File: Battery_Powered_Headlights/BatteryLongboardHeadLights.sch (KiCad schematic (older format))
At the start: 12 parts, among them U1 AL8805

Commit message: schematic changes nearly done
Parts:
- added C? (x6): C, symbol C
- added D?: D_Schottky, symbol D_Schottky
- added L?: L, symbol L
- added R? (x7): R, symbol R
- added U?: bq29700, MODULE, symbol bq29700
- added U?: MCP73833T, MODULE, symbol MCP73833T
- added U?: TPS55330RTER, MODULE, symbol TPS55330RTER
- added U?: DMN2040LTS-13, MODULE, symbol DMN2040LTS-13
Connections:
- net labels added: +BATT, SWITCH
- net labels removed: CTRL
- wire segments 44 -> 85
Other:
- note added: "Battery Charging and Regulation"
- note added: "Battery Protection"
- note added: "Fix this"
- note added: "LED Headlights"
- note removed: "Jumper to set control of LED's to either\nvoltage divider or external control (MCU)"
- note removed: "White LED Headlights"
- moved on the sheet: C1, C2, C3, C4, D1, D2, D4, L1, R1, R2, R3, U1

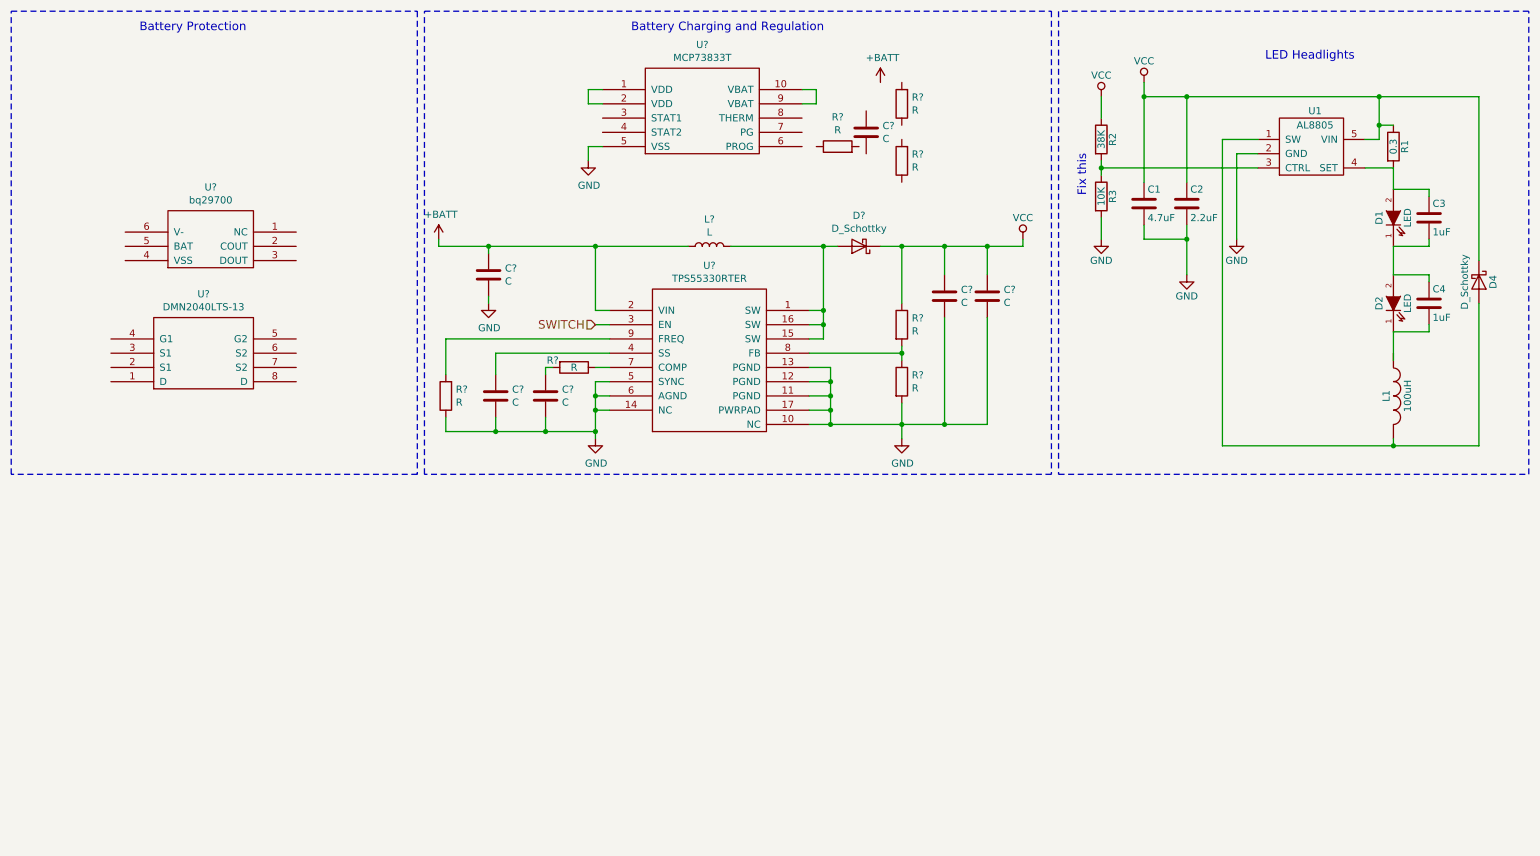
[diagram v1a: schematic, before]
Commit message: Schematic done, values almost, layout next
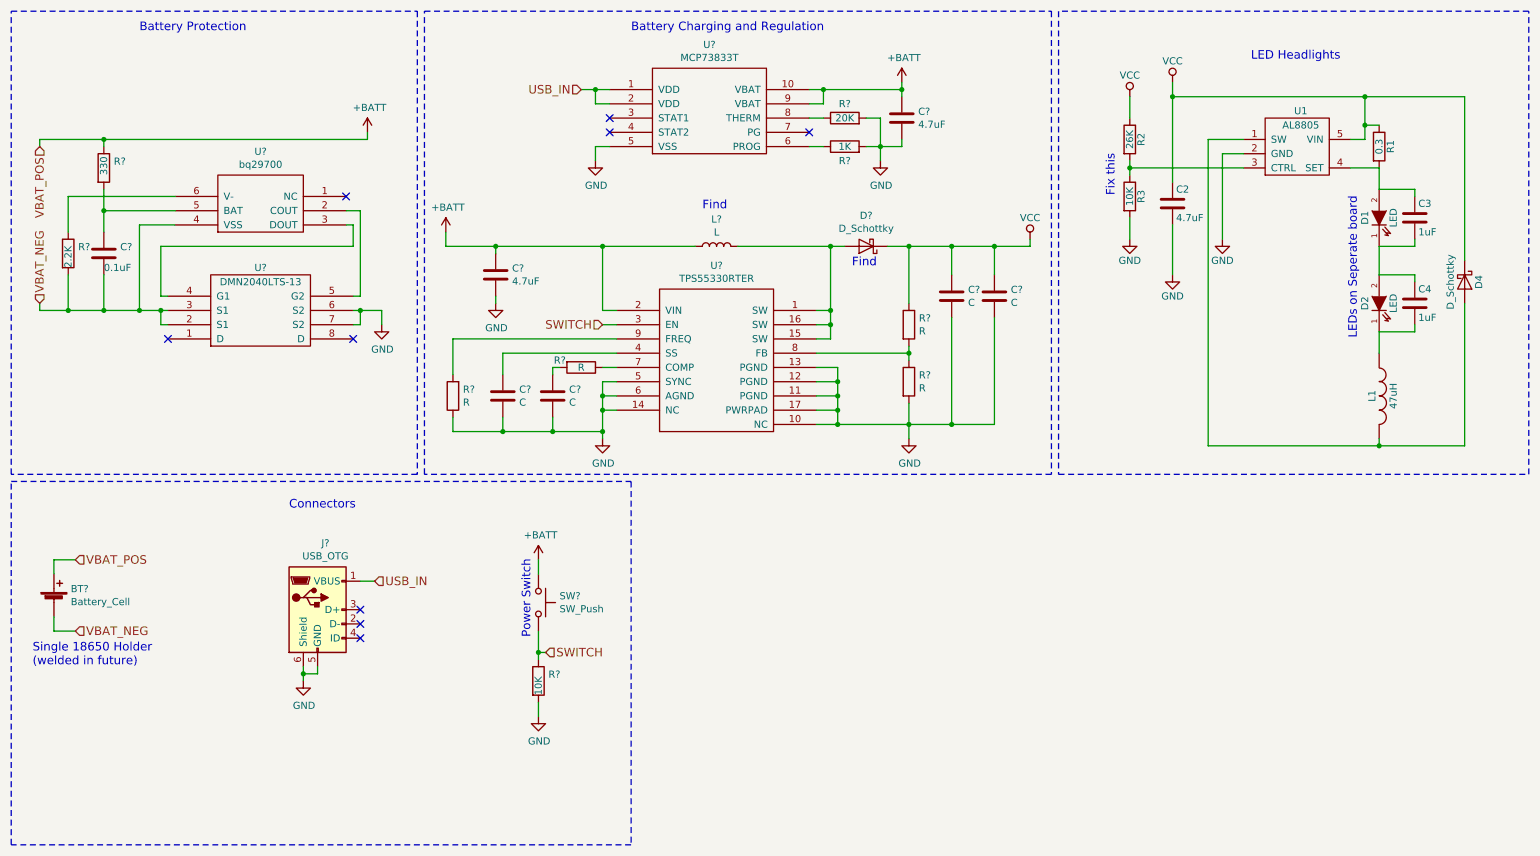
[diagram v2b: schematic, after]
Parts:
- removed C1: 4.7uF, Capacitors_SMD:C_0805, symbol C
- removed R?: R, symbol R
- removed U?: DMN2040LTS-13, MODULE, symbol DMN2040LTS-13
- added BT?: Battery_Cell, symbol Battery_Cell
- added C?: 0.1uF, symbol C
- added J?: USB_OTG, symbol USB_OTG
- added R?: 330, symbol R
- added R?: 2.2K, symbol R
- added R?: 10K, symbol R
- added SW?: SW_Push, symbol SW_Push
- added U?: DMN2040LTS-13, MODULE, symbol DMN2040LTS-13
- C2: value 2.2uF -> 4.7uF
- C? (x2): value C -> 4.7uF
- L1: value 100uH -> 47uH
- R2: value 38K -> 26K
- R?: value R -> 20K
- R?: value R -> 1K
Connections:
- net +BATT: now also C?.1, U?.10 (VBAT), U?.9 (VBAT), BT?.1 (+), R?.1, SW?.1
- net GND: now also C?.2, R?.2, R?.2, J?.5 (GND), J?.6 (Shield), R?.2, U?.6 (S2), U?.7 (S2)
- net SWITCH: now also R?.1, SW?.2
- net at C4.2, D2.1 (K): now also L1.1
- net at U?.2 (COUT): now also U?.5 (G2)
- net at U?.3 (DOUT): now also U?.4 (G1)
- net VBAT_NEG: now reaches U?.4 (VSS)
- net VBAT_NEG: now also BT?.2 (-), C?.2, R?.2, U?.2 (S1), U?.3 (S1)
- net at U?.5 (BAT): now also C?.1, R?.2
- net at U?.6 (V-): now also R?.1
- net USB_IN: now reaches U?.1 (VDD), U?.2 (VDD)
- net USB_IN: now also J?.1 (VBUS)
- net at U?.6 (PROG): now also R?.1
- net at U?.8 (THERM): now also R?.1
- no-connect marks 0 -> 9
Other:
- note added: "Connectors"
- note added: "Find"
- note added: "LEDs on Seperate board"
- note added: "Power Switch"
- note added: "Single 18650 Holder\n(welded in future)"
- moved on the sheet: C2, C3, C4, C?, D1, D2, D4, D?, L1, L?, R1, R2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

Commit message: schematic completed
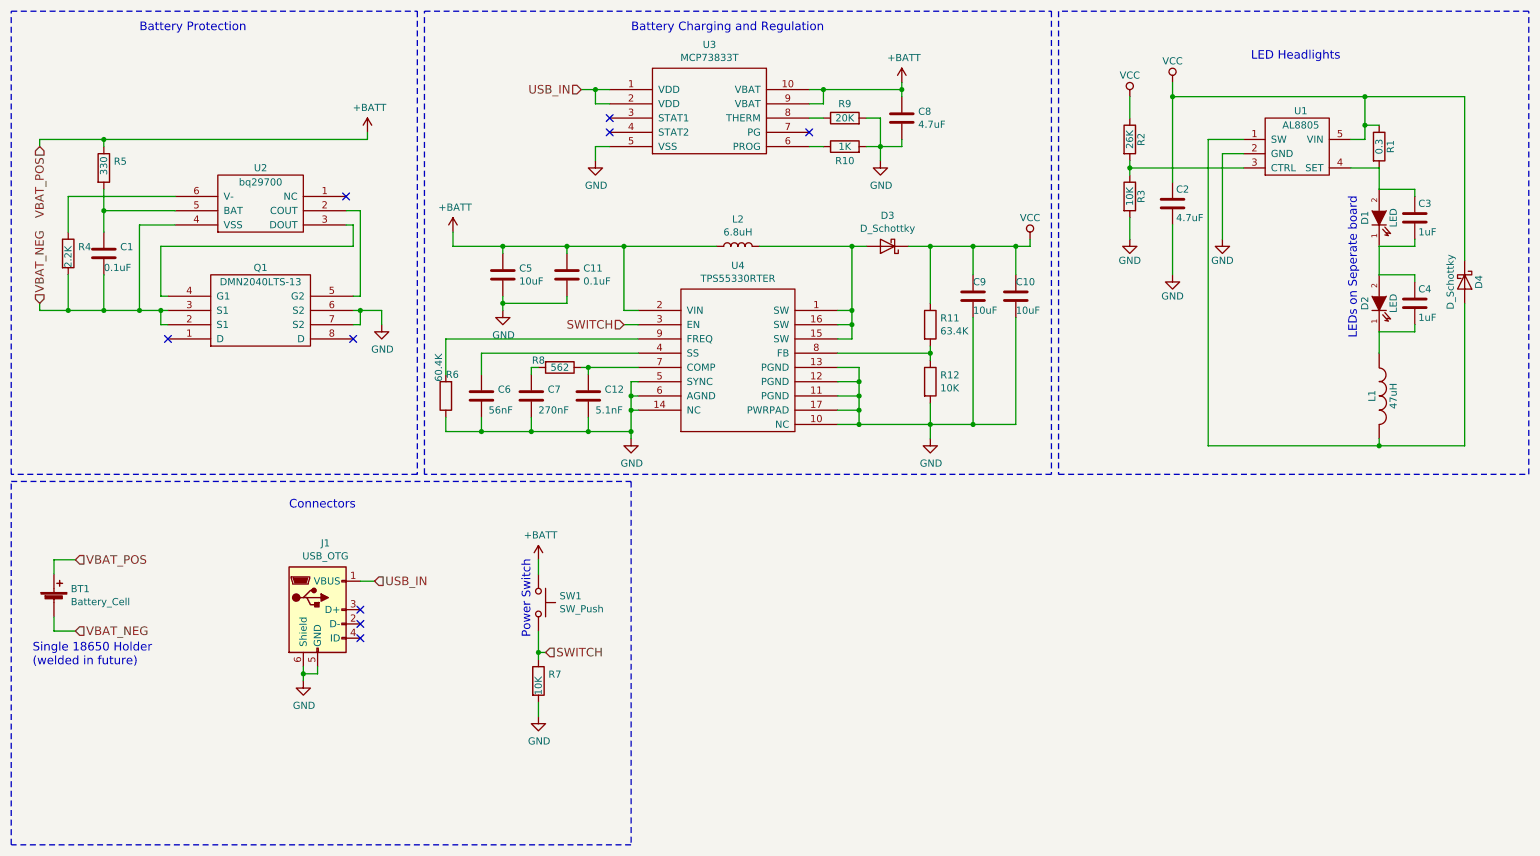
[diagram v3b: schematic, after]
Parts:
- added C11: 0.1uF, Capacitors_SMD:C_0603, symbol C
- added C12: 5.1nF, Capacitors_SMD:C_0603, symbol C
- BT1: renamed from BT?; footprint (none) -> Battery_Holders:Keystone_1042_1x18650
- C1: renamed from C?; footprint (none) -> Capacitors_SMD:C_0603
- C10, C9: renamed from C?; value C -> 10uF; footprint (none) -> Capacitors_SMD:C_0805
- C5: renamed from C?; value 4.7uF -> 10uF; footprint (none) -> Capacitors_SMD:C_0805
- C6: renamed from C?; value C -> 56nF; footprint (none) -> Capacitors_SMD:C_0603
- C7: renamed from C?; value C -> 270nF; footprint (none) -> Capacitors_SMD:C_0603
- C8: renamed from C?; footprint (none) -> Capacitors_SMD:C_0805
- D3: renamed from D?; footprint (none) -> Diodes_SMD:D_SOD-123F
- D4: footprint Light_Parts:PowerDI-123 -> Diodes_SMD:D_SOD-123F
- J1: renamed from J?; footprint (none) -> Connectors:USB_Micro-B
- L2: renamed from L?; value L -> 6.8uH; footprint (none) -> Light_Parts:Inductor_Bourns_6045
- Q1, U3: renamed from U?; footprint MODULE -> Housings_SSOP:TSSOP-8_4.4x3mm_Pitch0.65mm
- R10, R4, R5, R7, R9: renamed from R?; footprint (none) -> Resistors_SMD:R_0603
- R11: renamed from R?; value R -> 63.4K; footprint (none) -> Resistors_SMD:R_0603
- R12: renamed from R?; value R -> 10K; footprint (none) -> Resistors_SMD:R_0603
- R6: renamed from R?; value R -> 60.4K; footprint (none) -> Resistors_SMD:R_0603
- R8: renamed from R?; value R -> 562; footprint (none) -> Resistors_SMD:R_0603
- SW1: renamed from SW?; footprint (none) -> Light_Parts:GPTS203212B
- U2: renamed from U?; footprint MODULE -> Housings_SON:WSON6_1.5x1.5mm_Pitch0.5mm
- U4: renamed from U?; footprint MODULE -> Housings_DFN_QFN:DFN-10-1EP_3x3mm_Pitch0.5mm
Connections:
- net +BATT: now also C11.1
- net GND: now also C11.2, C12.2
- net at R8.1, U4.7 (COMP): now also C12.1
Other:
- note removed: "Find"
- note removed: "Fix this"
- moved on the sheet: C10, C5, C6, C7, C9, D3, L2, R11, R12, R6, R8, U4

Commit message: Schematic completed
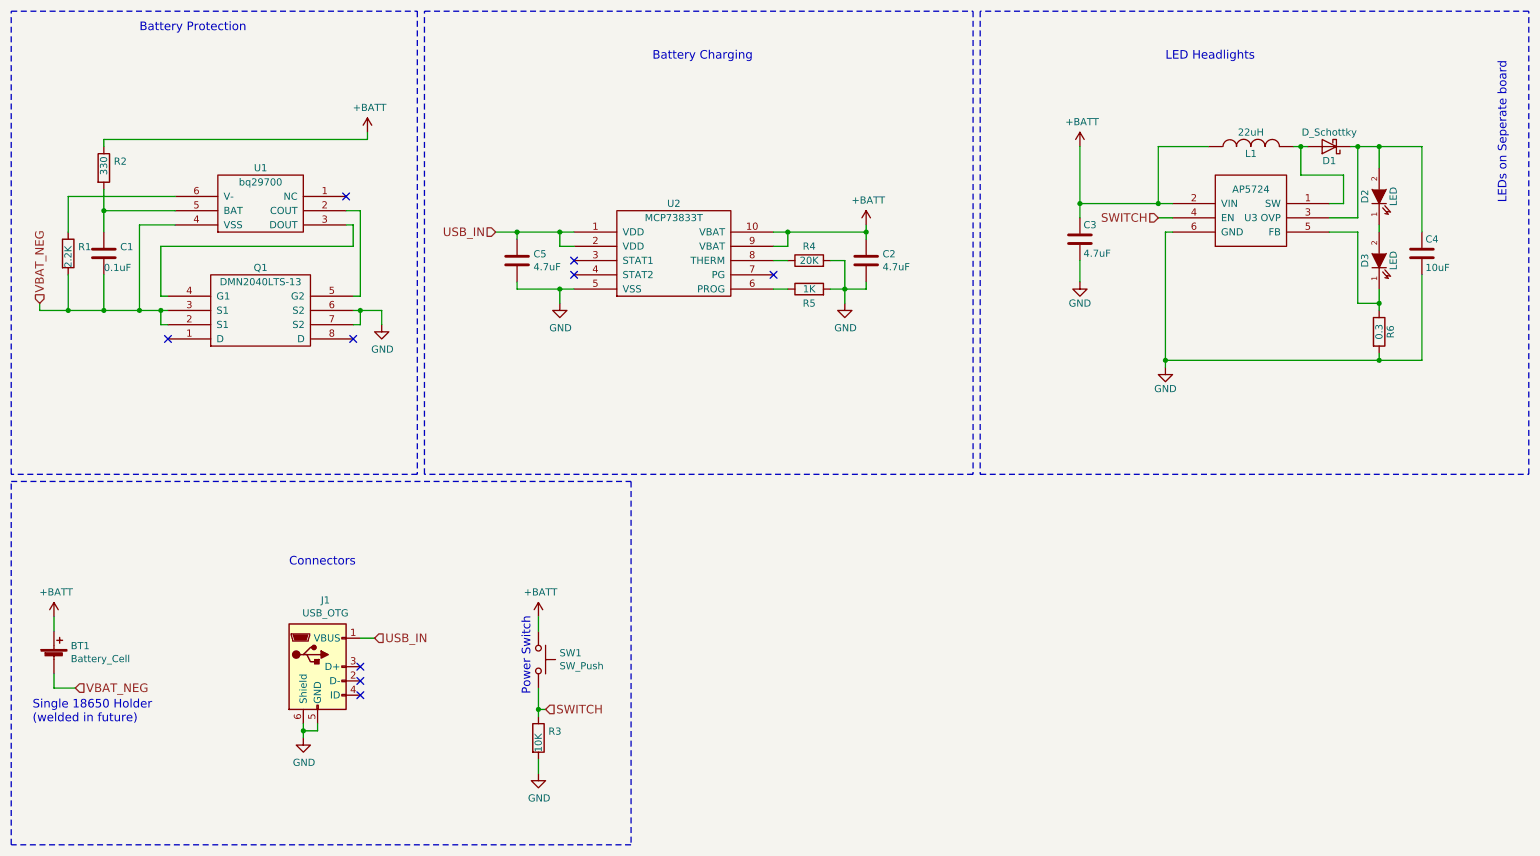
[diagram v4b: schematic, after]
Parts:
- removed C10, C9: 10uF, Capacitors_SMD:C_0805, symbol C
- removed C11: 0.1uF, Capacitors_SMD:C_0603, symbol C
- removed C12: 5.1nF, Capacitors_SMD:C_0603, symbol C
- removed C3: 1uF, Capacitors_SMD:C_0603, symbol C
- removed C6: 56nF, Capacitors_SMD:C_0603, symbol C
- removed C7: 270nF, Capacitors_SMD:C_0603, symbol C
- removed D3: D_Schottky, Diodes_SMD:D_SOD-123F, symbol D_Schottky
- removed L2: 6.8uH, Light_Parts:Inductor_Bourns_6045, symbol L
- removed R11: 63.4K, Resistors_SMD:R_0603, symbol R
- removed R12, R3: 10K, Resistors_SMD:R_0603, symbol R
- removed R2: 26K, Resistors_SMD:R_0603, symbol R
- removed R6: 60.4K, Resistors_SMD:R_0603, symbol R
- removed R8: 562, Resistors_SMD:R_0603, symbol R
- removed U1: AL8805, TO_SOT_Packages_SMD:SOT-23-5, symbol AL8805
- removed U4: TPS55330RTER, Housings_DFN_QFN:DFN-10-1EP_3x3mm_Pitch0.5mm, symbol TPS55330RTER
- added U3: AP5724, Housings_DFN_QFN:DFN-6-1EP_2x2mm_Pitch0.65mm, symbol AP5724
- C4: value 1uF -> 10uF
- C5: value 10uF -> 4.7uF
- D2: renamed from D1; footprint LEDs:LED-XP-G_CREE -> LEDs:LED_Cree-XP-G
- D3: renamed from D2; footprint LEDs:LED-XP-G_CREE -> LEDs:LED_Cree-XP-G
- L1: value 47uH -> 22uH; footprint Light_Parts:Inductor_Bourns_6045 -> Inductors_SMD:L_Taiyo-Yuden_NR-40xx
- R6: renamed from R1; footprint Resistors_SMD:R_0603 -> Resistors_SMD:R_0805
- U2: renamed from U3; footprint Housings_SSOP:TSSOP-8_4.4x3mm_Pitch0.65mm -> Housings_DFN_QFN:DFN-10-1EP_3x3mm_Pitch0.5mm
- renumbered C8 to C2, C2 to C3, D4 to D1, R4 to R1, R5 to R2, R7 to R3, R9 to R4, R10 to R5, U2 to U1
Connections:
- net +BATT: now also C3.1, L1.1, U3.2 (VIN); no longer C5.1
- net GND: now also C4.2, R6.2, U3.6 (GND)
- net SWITCH: now also U3.4 (EN)
- net USB_IN: now also C5.1
- net at D1.2 (A), L1.2: now also U3.1 (SW)
- net at D2.2 (A): now also C4.1, D1.1 (K), U3.3 (OVP); no longer R6.2
- net at D2.1 (K), D3.2 (A): no longer C4.1
- removed net VCC: C3.1, D1.1 (K), R6.1
- new net: D3.1 (K), R6.1, U3.5 (FB)
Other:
- note added: "Battery Charging"
- note removed: "Battery Charging and Regulation"
- moved on the sheet: BT1, C2, C3, D1, D2, D3, J1, L1, R3, R4, R5, R6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

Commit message: updating designs for newest revision; removing unneeded files
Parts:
- removed Q1: DMN2040LTS-13, Housings_SSOP:TSSOP-8_4.4x3mm_Pitch0.65mm, symbol DMN2040LTS-13
- added Q1: DMN2028UFDH-7, MODULE, symbol DMN2028UFDH-7
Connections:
- net GND: now also Q1.1 (S2)
- net VBAT_NEG: now also Q1.3 (S1)
- net at U1.2 (COUT): now also Q1.2 (G2)
- net at U1.3 (DOUT): now also Q1.4 (G1)
- no-connect marks 9 -> 11
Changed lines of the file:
@@
-	1    0    0    -1
-$EndComp
-$Comp
-L DMN2040LTS-13 Q1
-U 1 1 59F9D34F
-P 2250 3950
-F 0 "Q1" H 2250 4300 50  0000 C CNN
-F 1 "DMN2040LTS-13" H 2250 4200 50  0000 C CNN
-F 2 "Housings_SSOP:TSSOP-8_4.4x3mm_Pitch0.65mm" H 2400 3600 50  0001 C CNN
-F 3 "DOCUMENTATION" H 2250 3700 50  0001 C CNN
-	1    2250 3950
 	1    0    0    -1
 $EndComp
@@
 	700  3900 1600 3900
 Wire Wire Line
-	1600 4000 1550 4000
-Wire Wire Line
-	1550 4000 1550 3900
-Connection ~ 1550 3900
-Wire Wire Line
 	2900 3900 3100 3900
-Wire Wire Line
-	2950 3900 2950 4000
-Wire Wire Line
-	2950 4000 2900 4000
-Connection ~ 2950 3900
 NoConn ~ 2850 3100
 $Comp
@@
 	1150 2700 3000 2700
 $Comp
-L +BATT #PWR?
+L +BATT #PWR012
 U 1 1 5A07FB93
 P 800 6050
-F 0 "#PWR?" H 800 5900 50  0001 C CNN
+F 0 "#PWR012" H 800 5900 50  0001 C CNN
 F 1 "+BATT" H 815 6223 50  0000 C CNN
 F 2 "" H 800 6050 50  0001 C CNN
@@
 	1    0    0    -1
 $EndComp
+$Comp
+L DMN2028UFDH-7 Q1
+U 1 1 5A470564
+P 2250 3950
+F 0 "Q1" H 2250 4000 50  0000 C CNN
+F 1 "DMN2028UFDH-7" H 2250 4200 50  0000 C CNN
+F 2 "MODULE" H 2400 3600 50  0001 C CNN
+F 3 "DOCUMENTATION" H 2250 3700 50  0001 C CNN
+	1    2250 3950
+	1    0    0    -1
+$EndComp
+NoConn ~ 2900 4000
+NoConn ~ 1600 4000
 $EndSCHEMATC
